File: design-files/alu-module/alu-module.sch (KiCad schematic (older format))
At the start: 50 parts, among them U301 74HCT273, U302 74LS382A, U303 74HCT377, U304 74HCT245, U305 74HCT08, U306 74LS382A, U307 4002, U308 74HCT157, U309 74HCT157

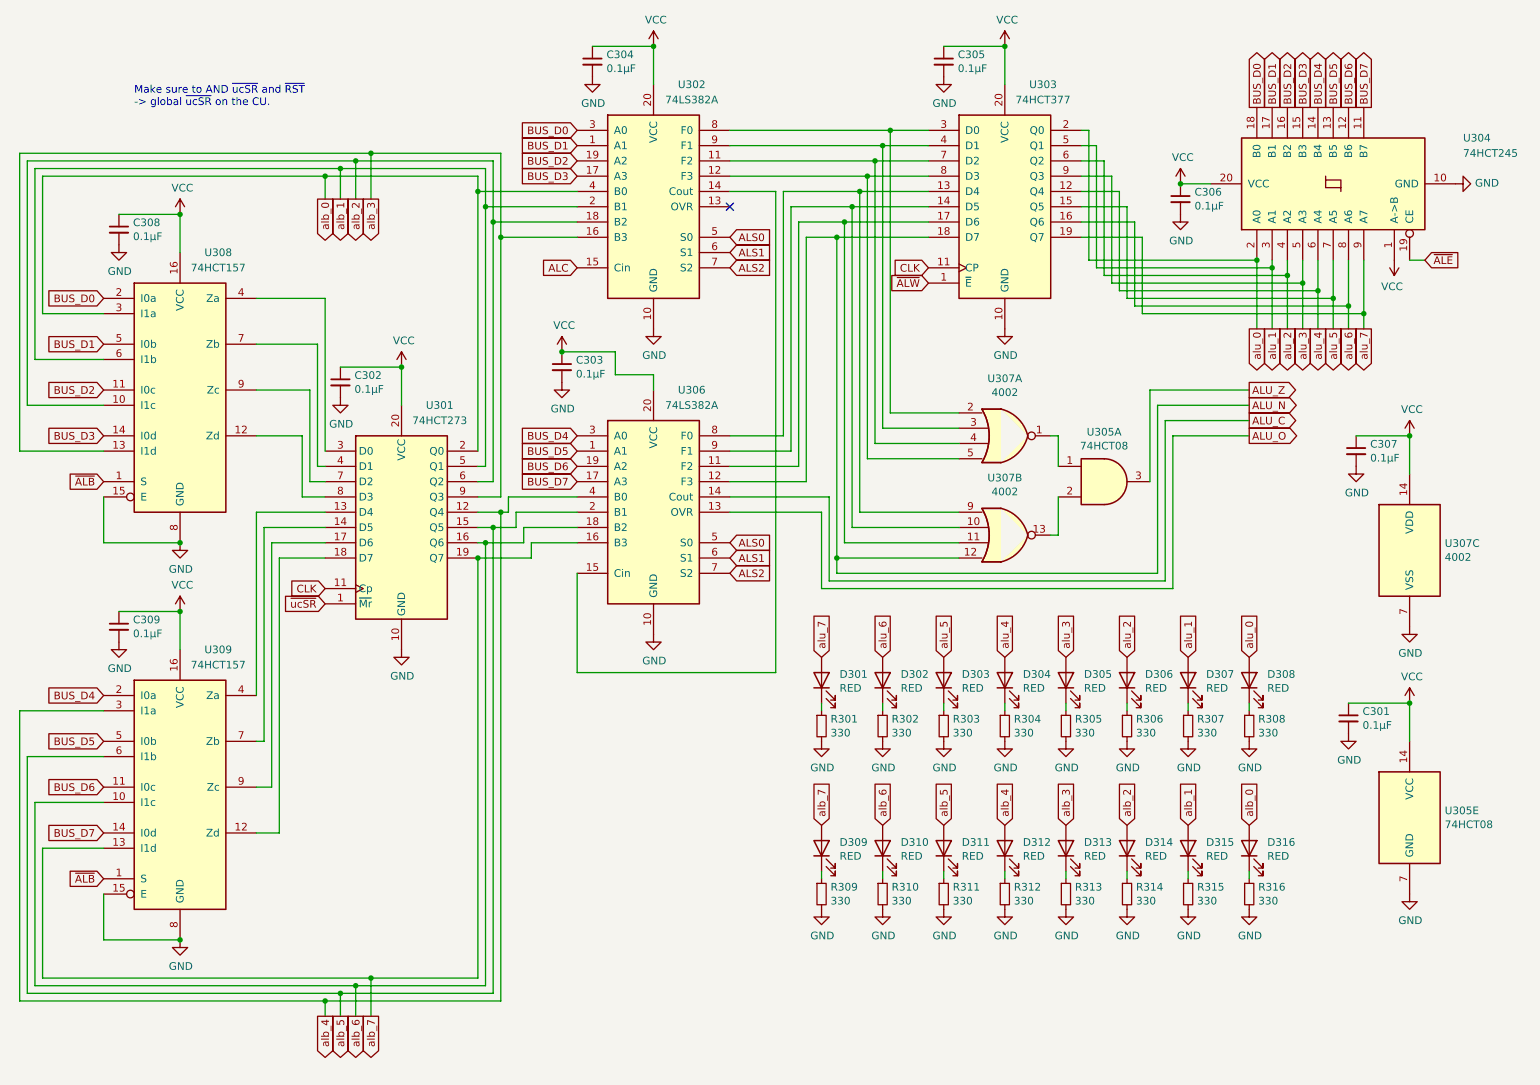
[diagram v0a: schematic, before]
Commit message: Use a pair of 74HCT161s as the ALU B register.  By just never having them count, we get all the behavior we want (gated clock for loading value + async reset).
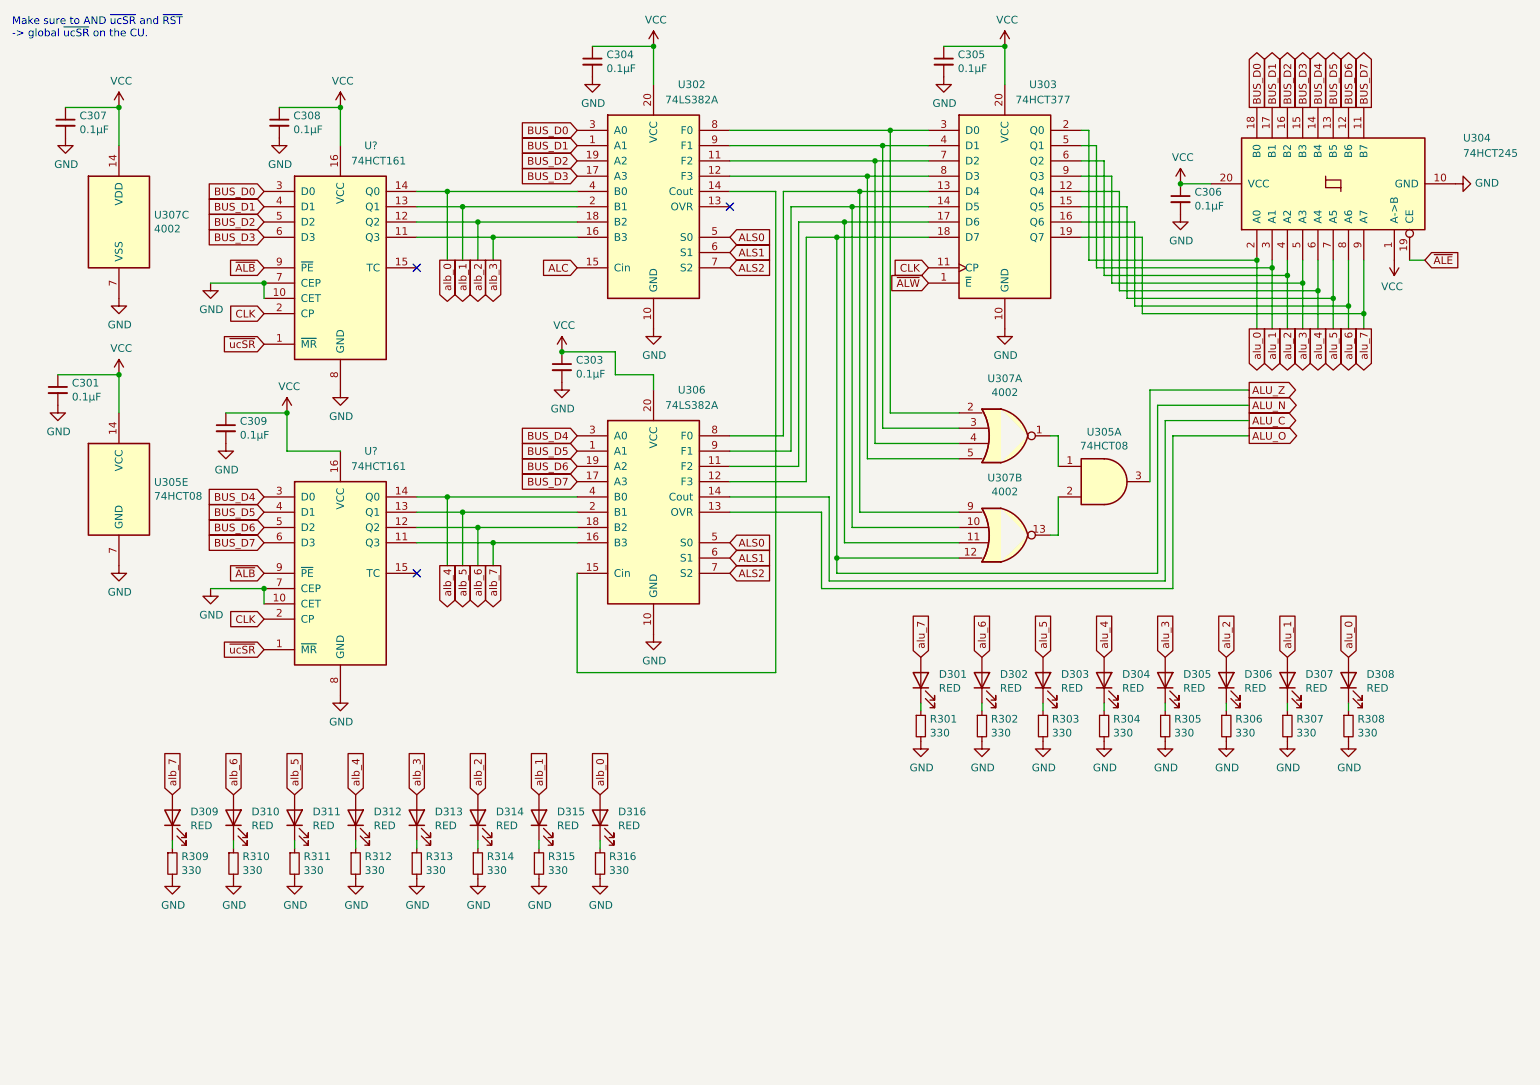
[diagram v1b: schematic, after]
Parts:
- removed C302: 0.1µF, Capacitor_THT:C_Radial_D6.3mm_H5.0mm_P2.50mm, symbol Device:C_Small
- removed U301: 74HCT273, Package_DIP:DIP-20_W7.62mm_Socket, symbol 74xx:74LS273
- removed U308, U309: 74HCT157, Package_DIP:DIP-16_W7.62mm_Socket, symbol 74xx:74LS157
- added U? (x2): 74HCT161, symbol 74xx:74LS161
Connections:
- net BUS_D0: now also U?.3 (D0)
- net BUS_D1: now also U?.4 (D1)
- net BUS_D2: now also U?.5 (D2)
- net BUS_D3: now also U?.6 (D3)
- net BUS_D4: now also U?.3 (D0)
- net BUS_D5: now also U?.4 (D1)
- net BUS_D6: now also U?.5 (D2)
- net BUS_D7: now also U?.6 (D3)
- net CLK: now also U?.2 (CP), U?.2 (CP)
- net GND: now also U?.10 (CET), U?.10 (CET), U?.7 (CEP), U?.7 (CEP), U?.8 (GND), U?.8 (GND)
- net VCC: now also U?.16 (VCC), U?.16 (VCC)
- net alb_0: now also U?.14 (Q0)
- net alb_1: now also U?.13 (Q1)
- net alb_2: now also U?.12 (Q2)
- net alb_3: now also U?.11 (Q3)
- net alb_4: now also U?.14 (Q0)
- net alb_5: now also U?.13 (Q1)
- net alb_6: now also U?.12 (Q2)
- net alb_7: now also U?.11 (Q3)
- net ~ALB: now also U?.9 (~PE), U?.9 (~PE)
- net ~ucSR: now also U?.1 (~MR), U?.1 (~MR)
- no-connect marks 1 -> 3
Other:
- moved on the sheet: C301, C307, C308, C309, D301, D302, D303, D304, D305, D306, D307, D308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
